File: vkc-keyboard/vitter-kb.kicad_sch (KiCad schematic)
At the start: 70 parts, among them SW1 SW_SPST, SW10 SW_SPST, SW11 SW_SPST, SW12 SW_SPST, SW13 SW_SPST, SW14 SW_SPST, SW15 SW_SPST, SW16 SW_SPST, SW17 SW_SPST, SW18 SW_SPST, SW19 SW_SPST, SW2 SW_SPST, SW20 SW_SPST, SW21 SW_SPST, SW22 SW_SPST, SW23 SW_SPST, SW24 SW_SPST, SW25 SW_SPST, SW26 SW_SPST, SW27 SW_SPST, SW28 SW_SPST, SW29 SW_SPST, SW3 SW_SPST, SW30 SW_SPST, SW31 SW_SPST, SW32 SW_SPST, SW33 SW_SPST, SW34 SW_SPST, SW35 SW_SPST, SW4 SW_SPST, SW5 SW_SPST, SW6 SW_SPST, SW7 SW_SPST, SW8 SW_SPST, SW9 SW_SPST

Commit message: bingo
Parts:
- added D36, D37, D38, D39: 1N4148, Keebio-Parts:Diode-dual, symbol Diode:1N4148
- added SW36, SW37, SW38, SW39: SW_SPST, vitter-kb:Kailh_socket_PG1350_reversible, symbol Switch:SW_SPST
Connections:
- net col1: now also SW36.2 (B)
- net col2: now also SW37.2 (B)
- net col3: now also SW38.2 (B)
- net col4: now also SW39.2 (B)
- new net: D39.2 (A), SW39.1 (A)
- new net: D36.2 (A), SW36.1 (A)
- new net: D38.2 (A), SW38.1 (A)
- new net: D37.2 (A), SW37.1 (A)
- new net row0: D36.1 (K), D37.1 (K), D38.1 (K), D39.1 (K)
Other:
- moved on the sheet: D1, D10, D11, D12, D13, D14, D15, D16, D17, D18, D19, D2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

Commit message: route
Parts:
- added H1, H2: MountingHole, MountingHole:MountingHole_2.2mm_M2, symbol Mechanical:MountingHole
- added J1, J2: TRRS, vitter-kb:TRRS-PJ-320A, symbol hillside:TRRS
- added U1: ProMicro_r, vitter-kb:ProMicro_v2, symbol hillside:ProMicro_r
- D1, D10, D11, D12, D13, D14, D15, D16, D17, D18, D19, D2, D20, D21, D22, D23, D24, D25, D26, D27, D28, D29, D3, D30, D31, D32, D33, D34, D35, D36, D37, D38, D39, D4, D5, D6, D7, D8, D9: footprint Keebio-Parts:Diode-dual -> vitter-kb:Diode-SOD-123-FB
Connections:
- net col1: now also U1.6 (SCL/D0/3)
- net col2: now also U1.7 (D4/4)
- net col3: now also U1.8 (C6/5)
- net col4: now also U1.9 (D7/6)
- net col5: now also U1.10 (E6/7)
- net col6: now also U1.11 (B4/8)
- net col7: now also U1.12 (B5/9)
- net row0: now also U1.20 (A3/F4)
- net row1: now also D2.2 (A), U1.19 (A2/F5); no longer D2.1 (K)
- net row2: now also U1.18 (A1/F6)
- net row3: now also U1.17 (A0/F7)
- net row4: now also U1.16 (15/B1)
- net row5: now also U1.15 (14/B3)
- net at SW2.1 (A): now also D2.1 (K); no longer D2.2 (A)
- new net +3.3V: J1.1 (Sleeve), J2.1 (Sleeve), U1.21 (VCC)
- new net GND: J1.2 (tip), J2.2 (tip), U1.23 (GND), U1.3 (GND), U1.4 (GND)
- new net row6: U1.14 (16/B2)
- new net rx: J1.4 (Ring2), J2.3 (Ring1), U1.2 (D2/RX1)
- new net tx: J1.3 (Ring1), J2.4 (Ring2), U1.1 (D3/TX0)
- no-connect marks 0 -> 4
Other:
- moved on the sheet: D2

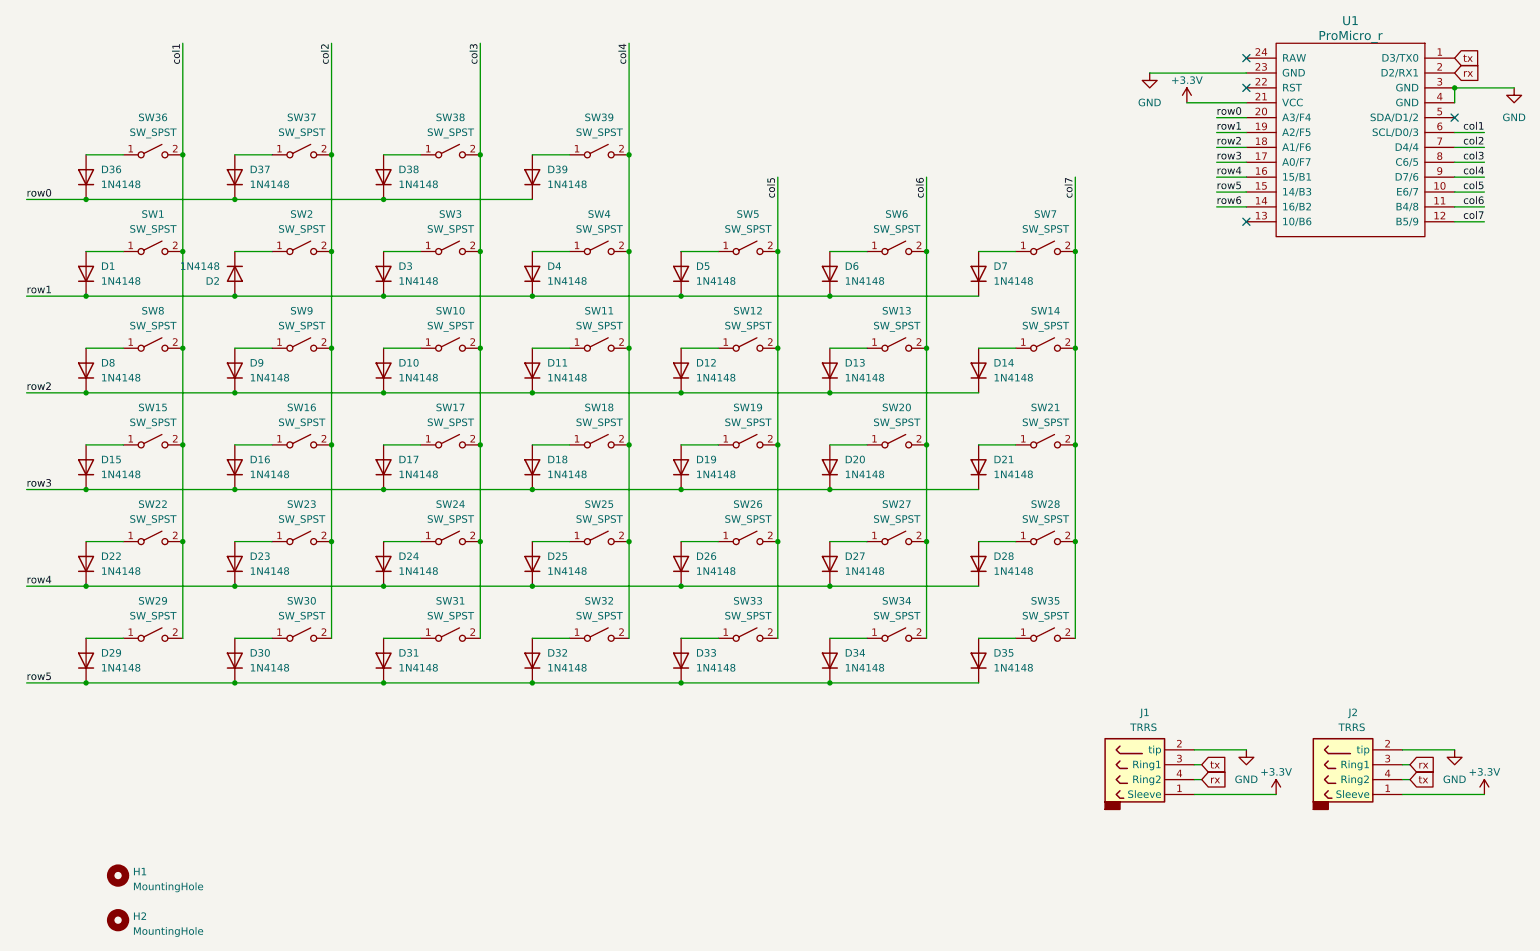
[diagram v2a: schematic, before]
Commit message: fix all DRC errors
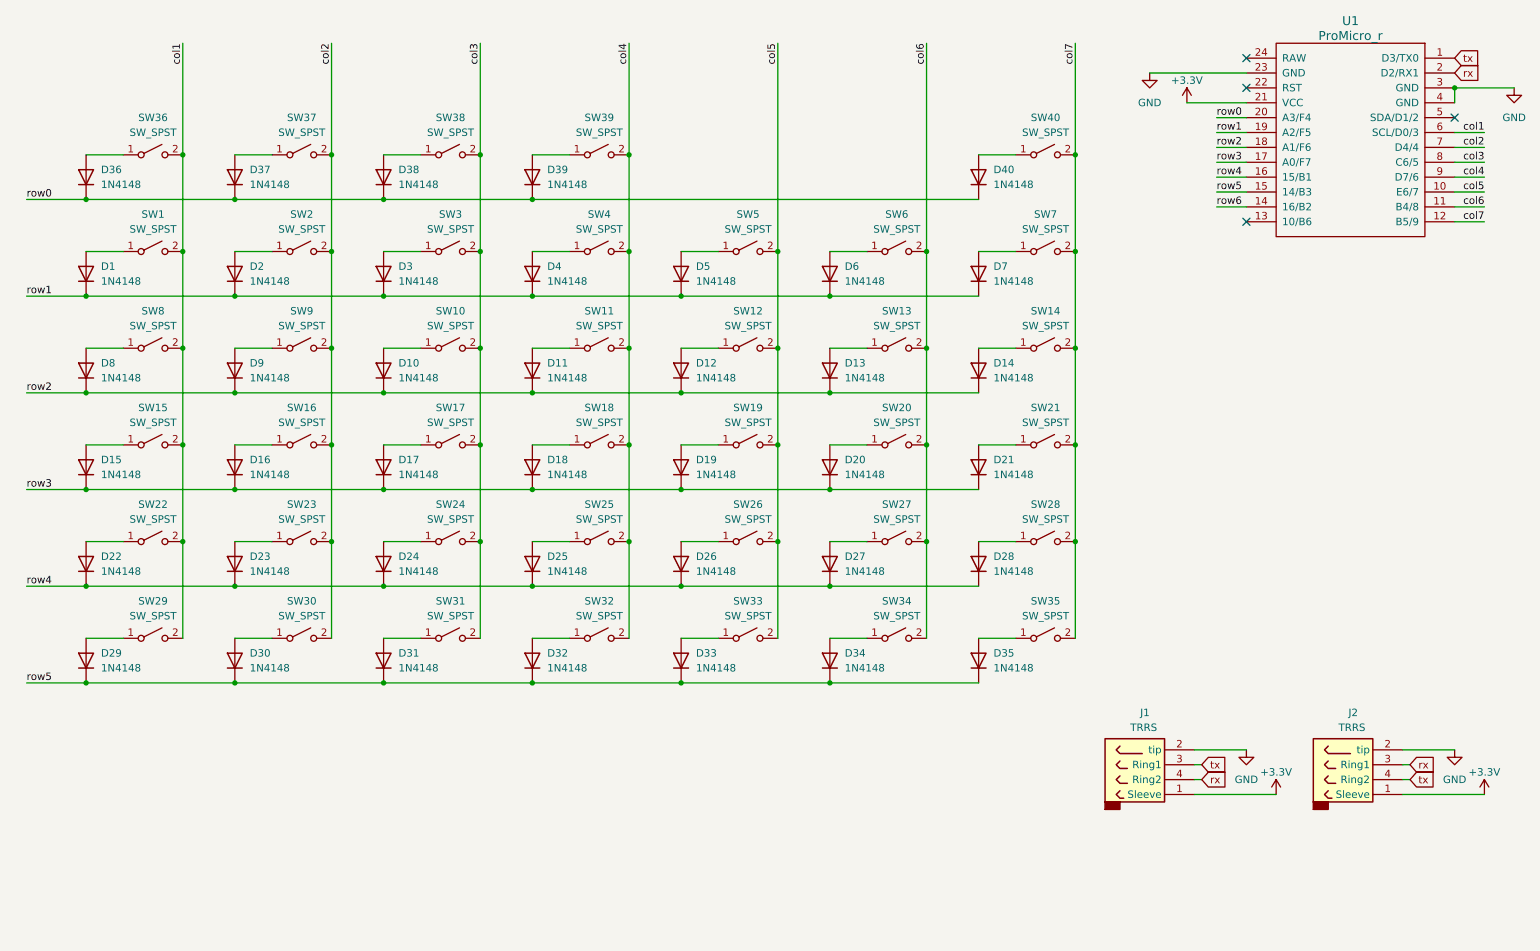
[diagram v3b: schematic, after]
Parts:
- removed H1, H2: MountingHole, MountingHole:MountingHole_2.2mm_M2, symbol Mechanical:MountingHole
- added D40: 1N4148, vitter-kb:Diode-SOD-123-FB, symbol Diode:1N4148
- added SW40: SW_SPST, vitter-kb:Kailh_socket_PG1350_reversible, symbol Switch:SW_SPST
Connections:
- net col7: now also SW40.2 (B)
- net row0: now also D40.1 (K)
- net row1: now also D2.1 (K); no longer D2.2 (A)
- net at SW2.1 (A): now also D2.2 (A); no longer D2.1 (K)
- new net: D40.2 (A), SW40.1 (A)
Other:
- moved on the sheet: D2
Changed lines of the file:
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@@
 	)
 	(junction
+		(at 204.47 44.45)
+		(diameter 0)
+		(color 0 0 0 0)
+	)
+	(junction
 		(at 86.36 101.6)
 		(diameter 0)
@@
 	)
 	(junction
-		(at 60.96 68.58)
-		(diameter 0)
-		(color 0 0 0 0)
-	)
-	(junction
 		(at 162.56 85.09)
 		(diameter 0)
@@
 	)
 	(junction
+		(at 60.96 68.58)
+		(diameter 0)
+		(color 0 0 0 0)
+	)
+	(junction
 		(at 86.36 134.62)
 		(diameter 0)
@@
 	)
 	(junction
+		(at 111.76 52.07)
+		(diameter 0)
+		(color 0 0 0 0)
+	)
+	(junction
 		(at 111.76 68.58)
 		(diameter 0)
@@
 	(wire
 		(pts
-			(xy 60.96 68.58) (xy 86.36 68.58)
-		)
-		(stroke
-			(width 0)
-			(type default)
-		)
-	)
-	(wire
-		(pts
 			(xy 128.27 93.98) (xy 128.27 110.49)
 		)
@@
 	(wire
 		(pts
-			(xy 204.47 48.26) (xy 204.47 60.96)
+			(xy 204.47 25.4) (xy 204.47 44.45)
 		)
 		(stroke
@@
 	(wire
 		(pts
+			(xy 187.96 44.45) (xy 194.31 44.45)
+		)
+		(stroke
+			(width 0)
+			(type default)
+		)
+	)
+	(wire
+		(pts
 			(xy 111.76 44.45) (xy 118.11 44.45)
 		)
@@
 	(wire
 		(pts
+			(xy 187.96 52.07) (xy 111.76 52.07)
+		)
+		(stroke
+			(width 0)
+			(type default)
+		)
+	)
+	(wire
+		(pts
 			(xy 128.27 44.45) (xy 128.27 60.96)
 		)
@@
 	(wire
 		(pts
-			(xy 179.07 48.26) (xy 179.07 60.96)
+			(xy 204.47 44.45) (xy 204.47 60.96)
+		)
+		(stroke
+			(width 0)
+			(type default)
+		)
+	)
+	(wire
+		(pts
+			(xy 179.07 25.4) (xy 179.07 60.96)
 		)
 		(stroke
@@
 	(wire
 		(pts
+			(xy 60.96 68.58) (xy 86.36 68.58)
+		)
+		(stroke
+			(width 0)
+			(type default)
+		)
+	)
+	(wire
+		(pts
 			(xy 128.27 25.4) (xy 128.27 44.45)
 		)
@@
 	(wire
 		(pts
-			(xy 153.67 48.26) (xy 153.67 60.96)
+			(xy 153.67 25.4) (xy 153.67 60.96)
 		)
 		(stroke
@@
 	)
 	(label "col6"
-		(at 179.07 48.26 270)
+		(at 179.07 25.4 270)
 		(fields_autoplaced yes)
 		(effects
@@
 	)
 	(label "col7"
-		(at 204.47 48.26 270)
+		(at 204.47 25.4 270)
 		(fields_autoplaced yes)
 		(effects
@@
 	)
 	(label "col5"
-		(at 153.67 48.26 270)
+		(at 153.67 25.4 270)
 		(fields_autoplaced yes)
 		(effects
@@
 	(symbol
 		(lib_id "Switch:SW_SPST")
+		(at 199.39 44.45 0)
+		(unit 1)
+		(exclude_from_sim no)
+		(in_bom yes)
+		(on_board yes)
+		(dnp no)
+		(property "Reference" "SW40"
+			(at 199.39 38.1 0)
+			(effects
+				(font
+					(size 1.27 1.27)
+				)
+			)
+		)
+		(property "Value" "SW_SPST"
+			(at 199.39 40.64 0)
+			(effects
+				(font
+					(size 1.27 1.27)
+				)
+			)
+		)
+		(property "Footprint" "vitter-kb:Kailh_socket_PG1350_reversible"
+			(at 199.39 44.45 0)
+			(effects
+				(font
+					(size 1.27 1.27)
+				)
+				(hide yes)
+			)
+		)
+		(property "Datasheet" "~"
+			(at 199.39 44.45 0)
+			(effects
+				(font
+					(size 1.27 1.27)
+				)
+				(hide yes)
+			)
+		)
+		(property "Description" ""
+			(at 199.39 44.45 0)
+			(effects
+				(font
+					(size 1.27 1.27)
+				)
+				(hide yes)
+			)
+		)
+		(pin "1"
+		)
+		(pin "2"
+		)
+		(instances
+			(project "vitter-kb"
+				(path "/e96a5538-5c73-4873-8878-70663283f154"
+					(reference "SW40")
+					(unit 1)
+				)
+			)
+		)
+	)
+	(symbol
+		(lib_id "Switch:SW_SPST")
 		(at 173.99 127 0)
 		(unit 1)
@@
 	)
 	(symbol
-		(lib_id "Mechanical:MountingHole")
-		(at 41.021 175.133 0)
-		(unit 1)
-		(exclude_from_sim no)
-		(in_bom yes)
-		(on_board yes)
-		(dnp no)
-		(fields_autoplaced yes)
-		(property "Reference" "H2"
-			(at 43.561 174.498 0)
-			(effects
-				(font
-					(size 1.27 1.27)
-				)
-				(justify left)
-			)
-		)
-		(property "Value" "MountingHole"
-			(at 43.561 177.038 0)
-			(effects
-				(font
-					(size 1.27 1.27)
-				)
-				(justify left)
-			)
-		)
-		(property "Footprint" "MountingHole:MountingHole_2.2mm_M2"
-			(at 41.021 175.133 0)
-			(effects
-				(font
-					(size 1.27 1.27)
-				)
-				(hide yes)
-			)
-		)
-		(property "Datasheet" "~"
-			(at 41.021 175.133 0)
-			(effects
-				(font
-					(size 1.27 1.27)
-				)
-				(hide yes)
-			)
-		)
-		(property "Description" ""
-			(at 41.021 175.133 0)
-			(effects
-				(font
-					(size 1.27 1.27)
-				)
-				(hide yes)
-			)
-		)
-		(instances
-			(project "vitter-kb"
-				(path "/e96a5538-5c73-4873-8878-70663283f154"
-					(reference "H2")
-					(unit 1)
-				)
-			)
-		)
-	)
-	(symbol
 		(lib_id "Switch:SW_SPST")
 		(at 173.99 60.96 0)
@@
 	)
 	(symbol
-		(lib_id "Mechanical:MountingHole")
-		(at 41.021 167.513 0)
-		(unit 1)
-		(exclude_from_sim no)
-		(in_bom yes)
-		(on_board yes)
-		(dnp no)
-		(fields_autoplaced yes)
-		(property "Reference" "H1"
-			(at 43.561 166.878 0)
-			(effects
-				(font
-					(size 1.27 1.27)
-				)
-				(justify left)
-			)
-		)
-		(property "Value" "MountingHole"
-			(at 43.561 169.418 0)
-			(effects
-				(font
-					(size 1.27 1.27)
-				)
-				(justify left)
-			)
-		)
-		(property "Footprint" "MountingHole:MountingHole_2.2mm_M2"
-			(at 41.021 167.513 0)
-			(effects
-				(font
-					(size 1.27 1.27)
-				)
-				(hide yes)
-			)
-		)
-		(property "Datasheet" "~"
-			(at 41.021 167.513 0)
-			(effects
-				(font
-					(size 1.27 1.27)
-				)
-				(hide yes)
-			)
-		)
-		(property "Description" ""
-			(at 41.021 167.513 0)
-			(effects
-				(font
-					(size 1.27 1.27)
-				)
-				(hide yes)
-			)
-		)
-		(instances
-			(project "vitter-kb"
-				(path "/e96a5538-5c73-4873-8878-70663283f154"
-					(reference "H1")
-					(unit 1)
-				)
-			)
-		)
-	)
-	(symbol
 		(lib_id "Switch:SW_SPST")
 		(at 72.39 44.45 0)
@@
 	(symbol
 		(lib_id "Diode:1N4148")
+		(at 187.96 48.26 90)
+		(unit 1)
+		(exclude_from_sim no)
+		(in_bom yes)
+		(on_board yes)
+		(dnp no)
+		(property "Reference" "D40"
+			(at 190.5 46.9899 90)
+			(effects
+				(font
+					(size 1.27 1.27)
+				)
+				(justify right)
+			)
+		)
+		(property "Value" "1N4148"
+			(at 190.5 49.5299 90)
+			(effects
+				(font
+					(size 1.27 1.27)
+				)
+				(justify right)
+			)
+		)
+		(property "Footprint" "vitter-kb:Diode-SOD-123-FB"
+			(at 158.75 45.72 0)
+			(effects
+				(font
+					(size 1.27 1.27)
+				)
+				(hide yes)
+			)
+		)
+		(property "Datasheet" "https://assets.nexperia.com/documents/data-sheet/1N4148_1N4448.pdf"
+			(at 187.96 48.26 0)
+			(effects
+				(font
+					(size 1.27 1.27)
+				)
+				(hide yes)
+			)
+		)
+		(property "Description" ""
+			(at 187.96 48.26 0)
+			(effects
+				(font
+					(size 1.27 1.27)
+				)
+				(hide yes)
+			)
+		)
+		(pin "1"
+		)
+		(pin "2"
+		)
+		(instances
+			(project "vitter-kb"
+				(path "/e96a5538-5c73-4873-8878-70663283f154"
+					(reference "D40")
+					(unit 1)
+				)
+			)
+		)
+	)
+	(symbol
+		(lib_id "Diode:1N4148")
 		(at 187.96 81.28 90)
 		(unit 1)
@@
 	(symbol
 		(lib_id "Diode:1N4148")
-		(at 60.96 64.77 270)
+		(at 60.96 64.77 90)
 		(unit 1)
 		(exclude_from_sim no)
@@
 		(dnp no)
 		(property "Reference" "D2"
-			(at 58.42 66.0401 90)
+			(at 63.5 63.4999 90)
 			(effects
 				(font
@@
 		)
 		(property "Value" "1N4148"
-			(at 58.42 63.5001 90)
+			(at 63.5 66.0399 90)
 			(effects
 				(font
@@
 		)
 		(property "Footprint" "vitter-kb:Diode-SOD-123-FB"
-			(at 90.17 67.31 0)
+			(at 31.75 62.23 0)
 			(effects
 				(font
